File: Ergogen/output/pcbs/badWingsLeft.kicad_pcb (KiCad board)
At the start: 2 copper layers, 149.9 x 112 mm, 152 parts

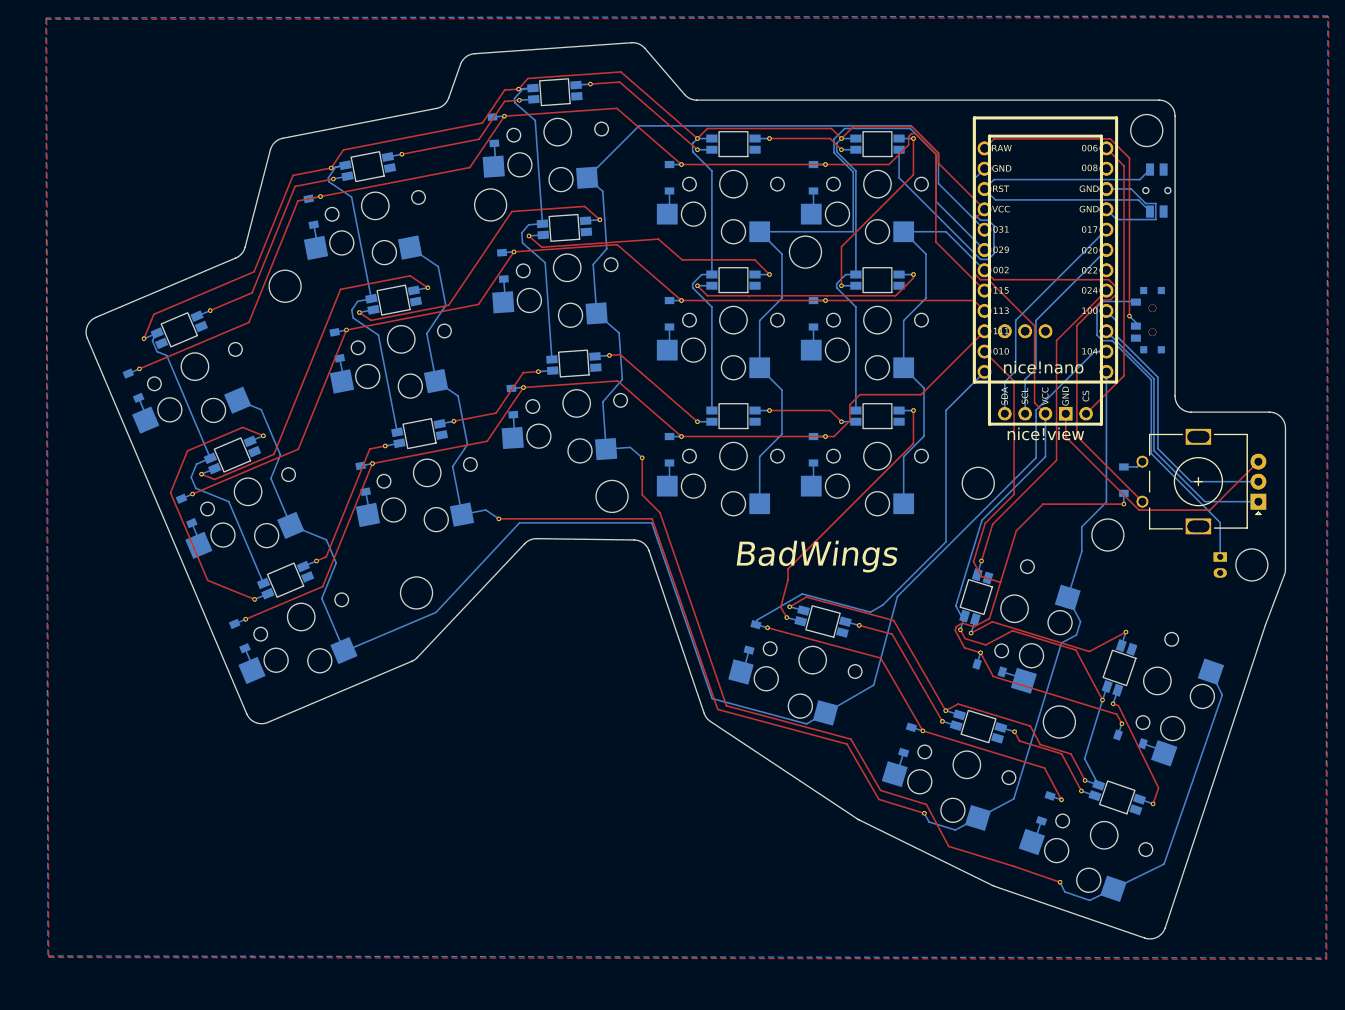
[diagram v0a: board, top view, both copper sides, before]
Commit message: Board v1.1 Complete
Complete prior to assembly
Case modifications could still be required
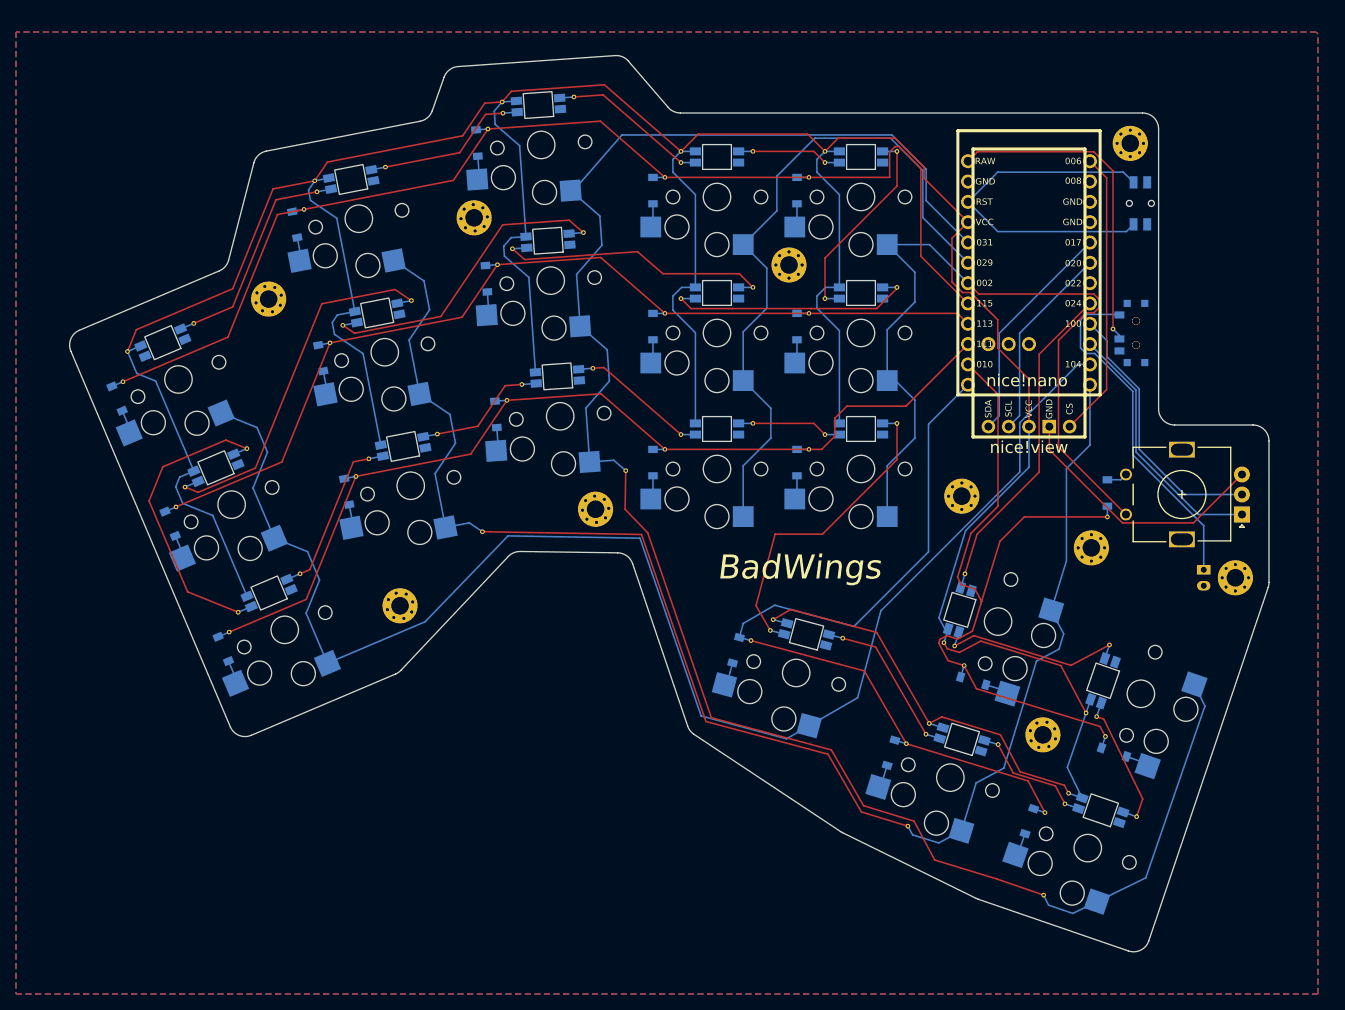
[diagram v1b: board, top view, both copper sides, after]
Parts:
- removed ? (x10): , HOLE_M2_TH
- removed the REF** at (181.2, 168.8)
- removed the REF** at (58.2, 151.9)
- removed the REF** at (176.4, 203.3)
- removed the REF** at (145.9, 141.5)
- removed the REF** at (136.9, 157.1)
- removed the REF** at (139.1, 182.9)
- removed the REF** at (115.7, 133.2)
- removed the REF** at (71.5, 183.2)
- removed the REF** at (143.9, 143.3)
- removed the REF** at (67.0, 144.6)
- removed the REF** at (143.9, 126.3)
- removed the REF** at (105.7, 118.3)
- removed the REF** at (73.7, 160.2)
- removed the REF** at (127.9, 158.5)
- removed the REF** at (91.0, 125.0)
- removed the REF** at (82.4, 128.1)
- removed the REF** at (94.2, 141.7)
- removed the REF** at (80.8, 130.3)
- removed the REF** at (127.9, 123.1)
- removed the REF** at (80.3, 175.9)
- removed the REF** at (85.7, 144.8)
- removed the REF** at (65.9, 165.0)
- removed the REF** at (156.3, 207.4)
- removed the REF** at (105.0, 137.2)
- removed the REF** at (97.5, 158.4)
- removed the REF** at (154.9, 140.1)
- removed the REF** at (167.6, 197.2)
- removed the REF** at (145.9, 158.5)
- removed the REF** at (103.1, 170.6)
- removed the REF** at (116.9, 150.2)
- removed the REF** at (58.7, 148.1)
- removed the REF** at (87.3, 163.7)
- removed the REF** at (175.9, 204.6)
- removed the REF** at (114.6, 116.3)
- removed the REF** at (125.9, 160.3)
- removed the REF** at (179.9, 193.7)
- removed the REF** at (158.6, 195.9)
- removed the REF** at (106.2, 154.2)
- removed the REF** at (64.8, 167.5)
- removed the REF** at (163.3, 187.3)
- removed the REF** at (145.9, 123.1)
- removed the REF** at (178.6, 193.3)
- removed the REF** at (103.8, 120.3)
- removed the REF** at (82.2, 126.7)
- removed the REF** at (125.9, 143.3)
- removed the REF** at (136.7, 184.2)
- removed the REF** at (184.9, 206.2)
- removed the REF** at (136.9, 123.1)
- removed the REF** at (125.9, 126.3)
- removed the REF** at (154.9, 157.1)
- removed the REF** at (106.9, 135.2)
- removed the REF** at (108.0, 152.2)
- removed the REF** at (159.0, 194.6)
- removed the REF** at (163.4, 175.9)
- removed the REF** at (121.0, 163.0)
- removed the REF** at (145.9, 124.5)
- removed the REF** at (160.8, 184.5)
- removed the REF** at (181.5, 184.8)
- removed the REF** at (139.5, 181.6)
- removed the REF** at (127.9, 141.5)
- removed the REF** at (127.9, 124.5)
- removed the REF** at (162.1, 184.9)
- removed the REF** at (181.0, 196.2)
- removed the REF** at (88.9, 161.5)
- removed the REF** at (156.1, 197.1)
- removed the REF** at (154.9, 123.1)
- removed the REF** at (181.9, 145.3)
- removed the REF** at (84.1, 147.0)
- removed the REF** at (173.3, 216.0)
- removed the REF** at (72.6, 180.7)
- removed the REF** at (105.6, 116.9)
- removed the REF** at (143.9, 160.3)
- removed the REF** at (136.9, 140.1)
- removed the REF** at (173.4, 205.7)
- removed the REF** at (148.2, 183.9)
- added REF**: VIA-0.6mm, VIA-0.6mm, F.Cu at (102.9, 138.8)
- added REF**: VIA-0.6mm, VIA-0.6mm, F.Cu at (101.1, 172.2)
- added REF**: VIA-0.6mm, VIA-0.6mm, F.Cu at (156.5, 197.5)
- added REF**: VIA-0.6mm, VIA-0.6mm, F.Cu at (92.2, 143.3)
- added REF**: VIA-0.6mm, VIA-0.6mm, F.Cu at (141.9, 144.9)
- added REF**: VIA-0.6mm, VIA-0.6mm, F.Cu at (161.3, 188.9)
- added REF**: VIA-0.6mm, VIA-0.6mm, F.Cu at (88.9, 126.6)
- added REF**: VIA-0.6mm, VIA-0.6mm, F.Cu at (63.9, 166.6)
- added REF**: VIA-0.6mm, VIA-0.6mm, F.Cu at (182.8, 207.8)
- added REF**: VIA-0.6mm, VIA-0.6mm, F.Cu at (152.9, 141.7)
- added REF**: VIA-0.6mm, VIA-0.6mm, F.Cu at (143.9, 126.1)
- added REF**: VIA-0.6mm, VIA-0.6mm, F.Cu at (179.2, 170.4)
- added REF**: VIA-0.6mm, VIA-0.6mm, F.Cu at (152.9, 158.7)
- added REF**: VIA-0.6mm, VIA-0.6mm, F.Cu at (103.5, 118.5)
- added REF**: VIA-0.6mm, VIA-0.6mm, F.Cu at (114.9, 151.8)
- added REF**: VIA-0.6mm, VIA-0.6mm, F.Cu at (165.5, 198.8)
- added REF**: VIA-0.6mm, VIA-0.6mm, F.Cu at (86.9, 163.1)
- added REF**: VIA-0.6mm, VIA-0.6mm, F.Cu at (69.4, 184.8)
- added REF**: VIA-0.6mm, VIA-0.6mm, F.Cu at (119.0, 164.6)
- added REF**: VIA-0.6mm, VIA-0.6mm, F.Cu at (143.9, 160.1)
- added REF**: VIA-0.6mm, VIA-0.6mm, F.Cu at (134.9, 141.7)
- added REF**: VIA-0.6mm, VIA-0.6mm, F.Cu at (158.7, 186.1)
- added REF**: VIA-0.6mm, VIA-0.6mm, F.Cu at (125.9, 124.7)
- added REF**: VIA-0.6mm, VIA-0.6mm, F.Cu at (141.9, 127.9)
- added REF**: VIA-0.6mm, VIA-0.6mm, F.Cu at (146.1, 185.5)
- added REF**: VIA-0.6mm, VIA-0.6mm, F.Cu at (82.0, 148.6)
- added REF**: VIA-0.6mm, VIA-0.6mm, F.Cu at (85.2, 165.3)
- added REF**: VIA-0.6mm, VIA-0.6mm, F.Cu at (56.7, 149.7)
- added REF**: VIA-0.6mm, VIA-0.6mm, F.Cu at (71.6, 161.8)
- added REF**: VIA-0.6mm, VIA-0.6mm, F.Cu at (171.4, 207.3)
- added REF**: VIA-0.6mm, VIA-0.6mm, F.Cu at (137.0, 184.6)
- added REF**: VIA-0.6mm, VIA-0.6mm, F.Cu at (156.9, 196.2)
- added REF**: VIA-0.6mm, VIA-0.6mm, F.Cu at (143.9, 124.7)
- added REF**: VIA-0.6mm, VIA-0.6mm, F.Cu at (173.9, 206.2)
- added REF**: VIA-0.6mm, VIA-0.6mm, F.Cu at (56.1, 153.5)
- added REF**: VIA-0.6mm, VIA-0.6mm, F.Cu at (65.0, 146.2)
- added REF**: VIA-0.6mm, VIA-0.6mm, F.Cu at (83.6, 146.4)
- added REF**: VIA-0.6mm, VIA-0.6mm, F.Cu at (70.5, 182.3)
- added REF**: VIA-0.6mm, VIA-0.6mm, F.Cu at (103.6, 119.9)
- added REF**: VIA-0.6mm, VIA-0.6mm, F.Cu at (141.9, 161.9)
- added REF**: VIA-0.6mm, VIA-0.6mm, F.Cu at (78.3, 177.5)
- added REF**: VIA-0.6mm, VIA-0.6mm, F.Cu at (134.9, 124.7)
- added REF**: VIA-0.6mm, VIA-0.6mm, F.Cu at (125.9, 126.1)
- added REF**: VIA-0.6mm, VIA-0.6mm, F.Cu at (101.7, 121.9)
- added REF**: VIA-0.6mm, VIA-0.6mm, F.Cu at (112.5, 117.9)
- added REF**: VIA-0.6mm, VIA-0.6mm, F.Cu at (113.7, 134.8)
- added REF**: VIA-0.6mm, VIA-0.6mm, F.Cu at (160.1, 186.5)
- added REF**: VIA-0.6mm, VIA-0.6mm, F.Cu at (134.6, 185.8)
- added REF**: VIA-0.6mm, VIA-0.6mm, F.Cu at (137.4, 183.2)
- added REF**: VIA-0.6mm, VIA-0.6mm, F.Cu at (179.9, 146.9)
- added REF**: VIA-0.6mm, VIA-0.6mm, F.Cu at (179.4, 186.4)
- added REF**: VIA-0.6mm, VIA-0.6mm, F.Cu at (154.2, 209.0)
- added REF**: VIA-0.6mm, VIA-0.6mm, F.Cu at (176.5, 194.9)
- added REF**: VIA-0.6mm, VIA-0.6mm, F.Cu at (161.4, 177.5)
- added REF**: VIA-0.6mm, VIA-0.6mm, F.Cu at (174.3, 204.9)
- added REF**: VIA-0.6mm, VIA-0.6mm, F.Cu at (104.8, 136.9)
- added REF**: VIA-0.6mm, VIA-0.6mm, F.Cu at (154.0, 198.7)
- added REF**: VIA-0.6mm, VIA-0.6mm, F.Cu at (123.9, 161.9)
- added REF**: VIA-0.6mm, VIA-0.6mm, F.Cu at (171.2, 217.6)
- added REF**: VIA-0.6mm, VIA-0.6mm, F.Cu at (80.1, 128.4)
- added REF**: VIA-0.6mm, VIA-0.6mm, F.Cu at (95.4, 160.0)
- added REF**: VIA-0.6mm, VIA-0.6mm, F.Cu at (104.1, 155.8)
- added REF**: VIA-0.6mm, VIA-0.6mm, F.Cu at (123.9, 144.9)
- added REF**: VIA-0.6mm, VIA-0.6mm, F.Cu at (143.9, 143.1)
- added REF**: VIA-0.6mm, VIA-0.6mm, F.Cu at (125.9, 143.1)
- added REF**: VIA-0.6mm, VIA-0.6mm, F.Cu at (152.9, 124.7)
- added REF**: VIA-0.6mm, VIA-0.6mm, F.Cu at (80.4, 129.7)
- added REF**: VIA-0.6mm, VIA-0.6mm, F.Cu at (62.8, 169.1)
- added REF**: VIA-0.6mm, VIA-0.6mm, F.Cu at (134.9, 158.7)
- added REF**: VIA-0.6mm, VIA-0.6mm, F.Cu at (106.0, 153.8)
- added REF**: VIA-0.6mm, VIA-0.6mm, F.Cu at (178.9, 197.8)
- added REF**: VIA-0.6mm, VIA-0.6mm, F.Cu at (125.9, 160.1)
- added REF**: VIA-0.6mm, VIA-0.6mm, F.Cu at (177.8, 195.3)
- added REF**: VIA-0.6mm, VIA-0.6mm, F.Cu at (123.9, 127.9)
- added REF**: VIA-0.6mm, VIA-0.6mm, F.Cu at (78.8, 131.9)
- added _76: , MountingHole_2.2mm_M2_Pad_Via, F.Cu at (171.1, 197.6)
- added _77: , MountingHole_2.2mm_M2_Pad_Via, F.Cu at (90.8, 181.5)
- added _78: , MountingHole_2.2mm_M2_Pad_Via, F.Cu at (74.3, 143.1)
- added _79: , MountingHole_2.2mm_M2_Pad_Via, F.Cu at (139.4, 138.9)
- added _80: , MountingHole_2.2mm_M2_Pad_Via, F.Cu at (195.2, 178.0)
- added _81: , MountingHole_2.2mm_M2_Pad_Via, F.Cu at (115.2, 169.4)
- added _82: , MountingHole_2.2mm_M2_Pad_Via, F.Cu at (100.0, 133.0)
- added _83: , MountingHole_2.2mm_M2_Pad_Via, F.Cu at (161.0, 167.8)
- added _84: , MountingHole_2.2mm_M2_Pad_Via, F.Cu at (177.2, 174.2)
- added _85: , MountingHole_2.2mm_M2_Pad_Via, F.Cu at (182.0, 123.7)
- moved LED19 2.61 mm to (178.3, 207.0)
- moved S14 2.61 mm to (148.4, 147.4)
- moved D19 2.61 mm to (169.4, 208.4)
- moved B1 2.61 mm to (183.3, 131.2)
- moved D4 2.61 mm to (84.1, 167.2)
- moved niceView1 2.61 mm to (169.4, 160.4)
- moved S4 2.61 mm to (92.1, 166.5)
- moved D17 2.61 mm to (152.1, 199.9)
- moved D7 2.61 mm to (102.7, 157.5)
- moved LED4 2.61 mm to (91.1, 161.6)
- moved D8 2.61 mm to (101.6, 140.6)
- moved LED15 2.61 mm to (148.4, 125.4)
- moved LED16 2.61 mm to (141.6, 185.0)
- moved S8 2.61 mm to (109.6, 140.8)
- moved S15 2.61 mm to (148.4, 130.4)
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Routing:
- net GND: track 81.6 -> 33.3 mm
- net P029: track 92.0 -> 85.4 mm
- net LED5: track 36.3 -> 40.1 mm
- net P031: track 226.6 -> 229.0 mm
- net P002: track 100.6 -> 102.7 mm
- net RST: track 43.6 -> 45.4 mm
- net VCC: track 485.6 -> 487.2 mm
- net P115: track 147.8 -> 149.1 mm
- net LED10: track 37.8 -> 38.8 mm
- net P104: track 181.9 -> 182.7 mm
- net P100: track 34.2 -> 33.4 mm
- net P011: track 33.1 -> 32.4 mm
- net P106: track 188.8 -> 189.5 mm
- net P010: track 95.2 -> 95.8 mm
- net P009: track 102.2 -> 102.8 mm
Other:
- outline, holes or cut-outs redrawn
